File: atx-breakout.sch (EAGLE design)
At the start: 2 parts

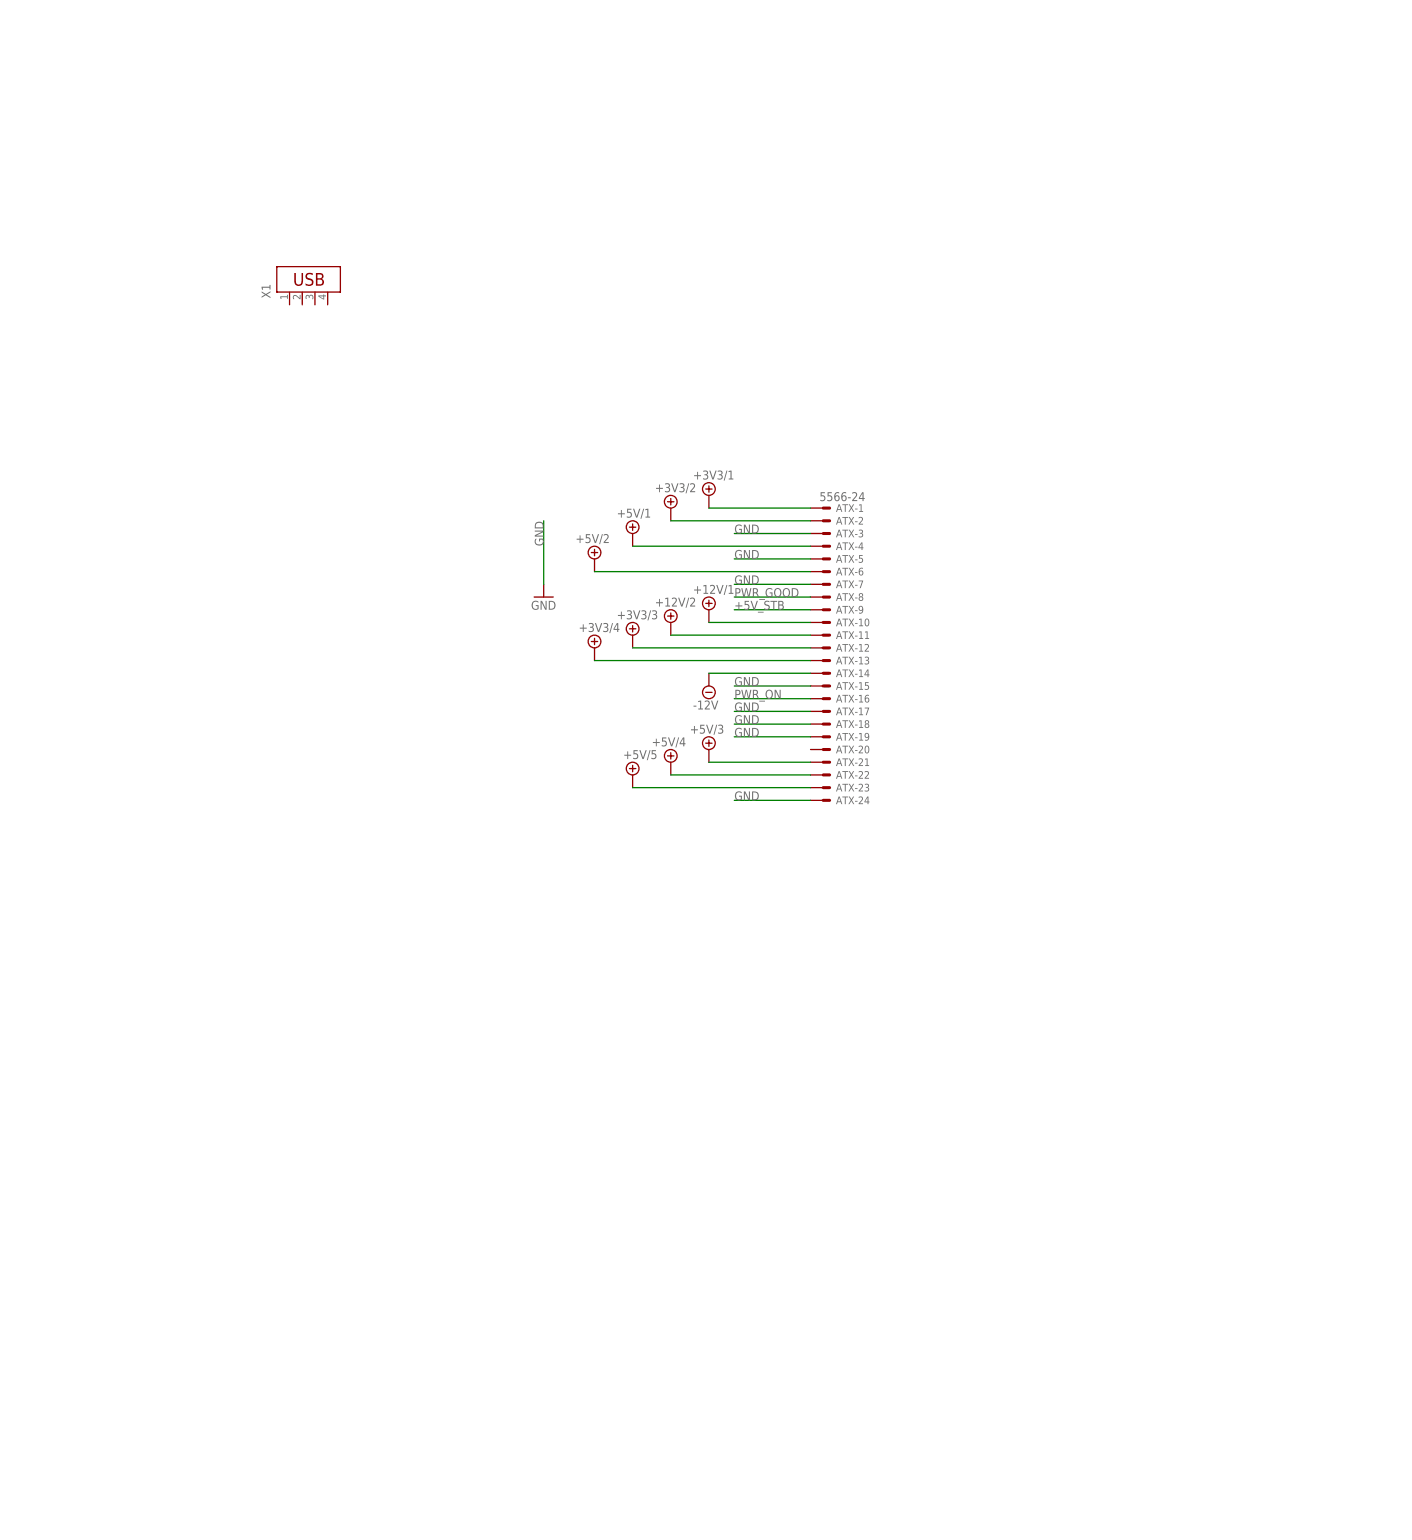
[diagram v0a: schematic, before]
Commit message: Six channel version, initial layout
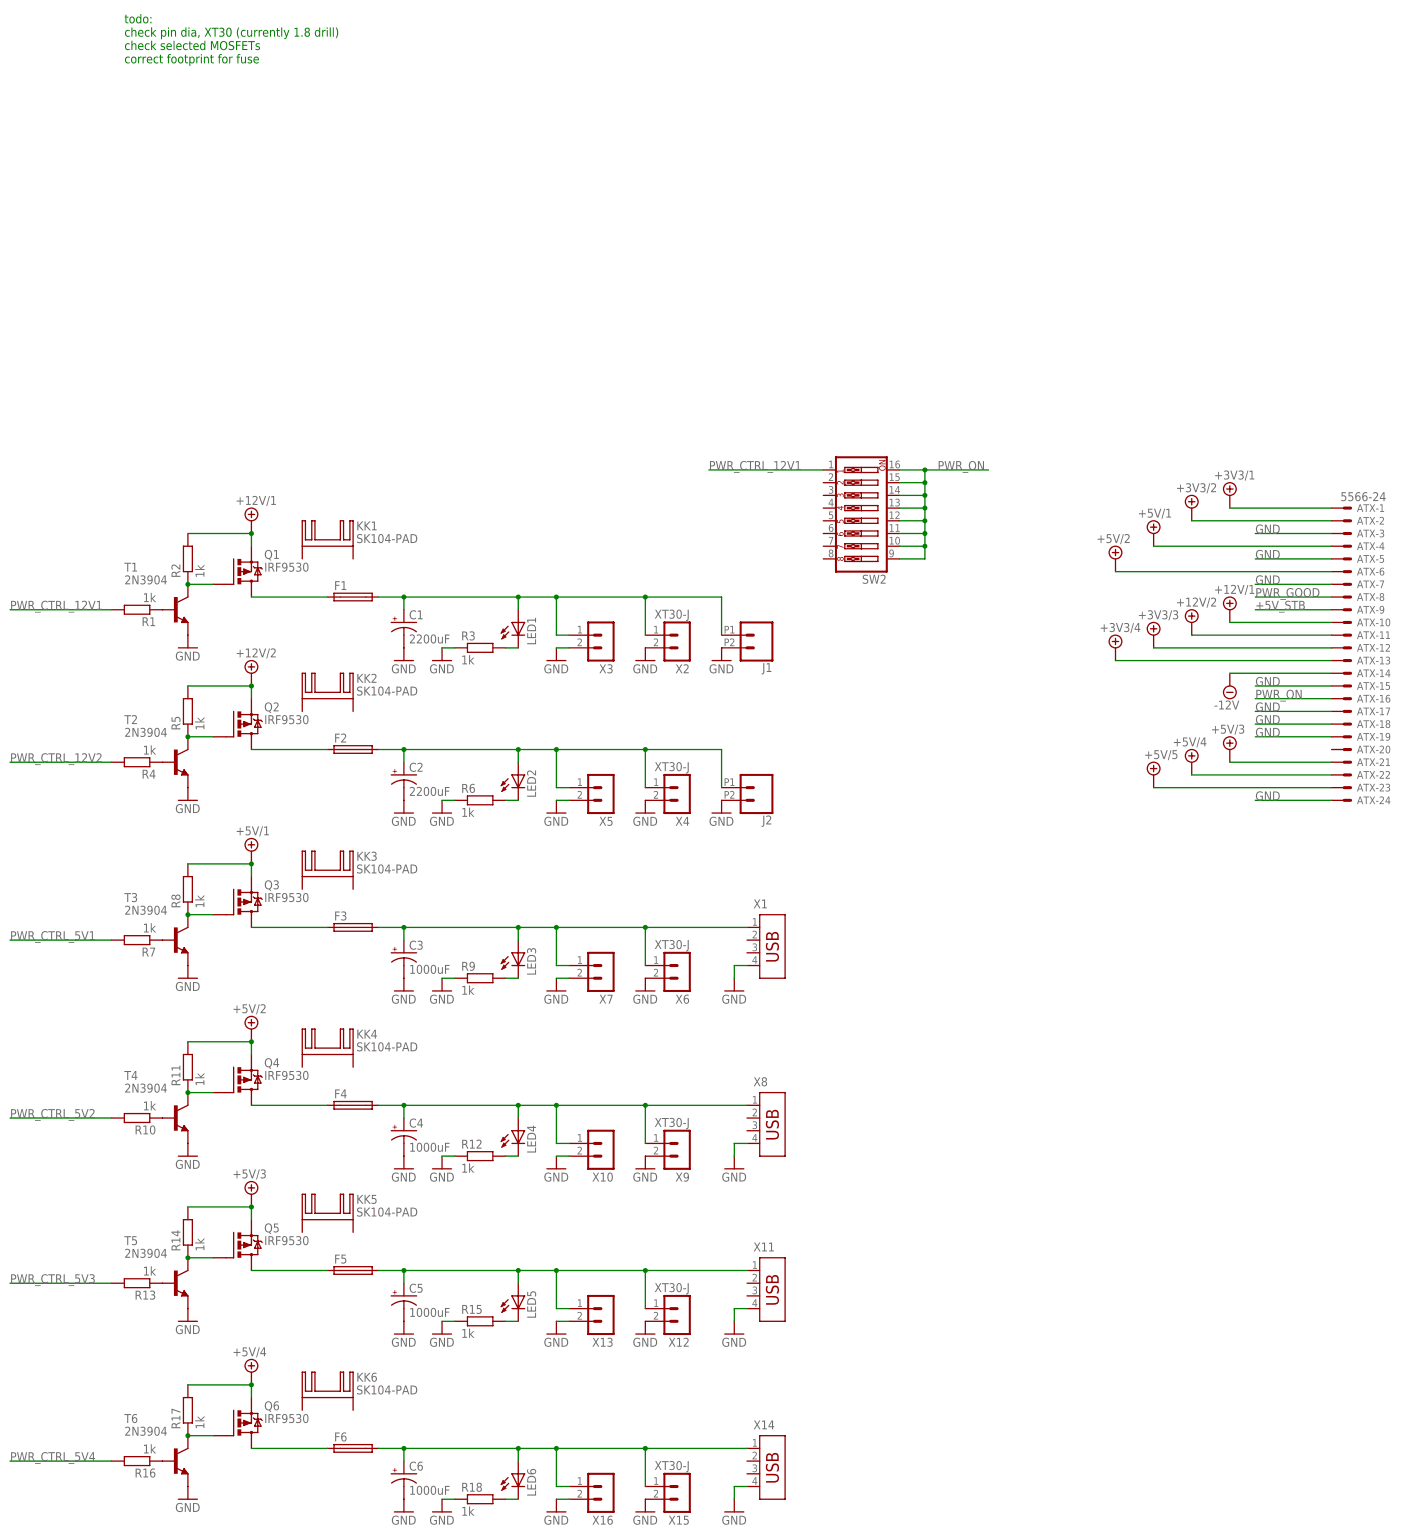
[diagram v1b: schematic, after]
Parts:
- added C1, C2: 2200uF, rcl:CPOL-USE7.5-16
- added C3, C4, C5, C6: 1000uF, rcl:CPOL-USE5-10.5
- added F1, F2, F3, F4, F5, F6: (no value), fuse:LITTLEFUSE
- added J1, J2: (no value), SparkFun-Connectors:CONN_022.54MM_SCREWTERM
- added KK1, KK2, KK3, KK4, KK5, KK6: SK104-PAD, heatsink:SK104-PAD
- added LED1, LED2, LED3, LED4, LED5, LED6: (no value), joakim:LED_J3MM
- added Q1, Q2, Q3, Q4, Q5, Q6: IRF9530, transistor-power:IRF9530
- added R1, R10, R11, R12, R13, R14, R15, R16, R17, R18, R2, R3, R4, R5, R6, R7, R8, R9: 1k, rcl:R-EU_0207/7
- added SW2: (no value), special:SW_DIP-8
- added T1, T2, T3, T4, T5, T6: 2N3904, transistor:2N3904
- added X10, X13, X16, X3, X5, X7: MA02-1JC, joakim:MA02-1JC
- added X11, X14, X8: (no value), con-amp:USB-787616
- added X12, X15, X2, X4, X6, X9: XT30-J, joakim:XT30-J
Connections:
- new net N$1: R1.1, T1.B
- new net N$10: LED2.C, R6.2
- new net N$11: F2.1, Q2.D
- new net N$12: R7.1, T3.B
- new net N$13: Q3.G, R8.1, T3.C
- new net N$14: C3.+, F3.2, LED3.A, X1.1, X6.1, X7.1
- new net N$15: LED3.C, R9.2
- new net N$16: F3.1, Q3.D
- new net N$17: R10.1, T4.B
- new net N$18: Q4.G, R11.1, T4.C
- new net N$19: C4.+, F4.2, LED4.A, X10.1, X8.1, X9.1
- new net N$2: Q1.G, R2.1, T1.C
- new net N$20: LED4.C, R12.2
- new net N$21: F4.1, Q4.D
- new net N$22: R13.1, T5.B
- new net N$23: Q5.G, R14.1, T5.C
- new net N$24: C5.+, F5.2, LED5.A, X11.1, X12.1, X13.1
- new net N$25: LED5.C, R15.2
- new net N$26: F5.1, Q5.D
- new net N$27: R16.1, T6.B
- new net N$28: Q6.G, R17.1, T6.C
- new net N$29: C6.+, F6.2, LED6.A, X14.1, X15.1, X16.1
- new net N$3: Q1.S, R2.2
- new net N$30: LED6.C, R18.2
- new net N$31: F6.1, Q6.D
- new net N$4: C1.+, F1.2, J1.1, LED1.A, X2.1, X3.1
- new net N$5: LED1.C, R3.2
- new net N$6: F1.1, Q1.D
- new net N$7: R4.1, T2.B
- new net N$8: Q2.G, R5.1, T2.C
- new net N$9: C2.+, F2.2, J2.1, LED2.A, X4.1, X5.1
- new net PWR_CTRL_12V1: R1.2, SW2.1
- new net PWR_CTRL_12V2: R4.2
- new net PWR_CTRL_5V1: R7.2
- new net PWR_CTRL_5V2: R10.2
- new net PWR_CTRL_5V3: R13.2
- new net PWR_CTRL_5V4: R16.2
- net +5V/1: now also Q2.S, Q3.S, R5.2, R8.2
- net +5V/2: now also Q4.S, R11.2
- net +5V/3: now also Q5.S, R14.2
- net +5V/4: now also Q6.S, R17.2
- net GND: now also C1.-, C2.-, C3.-, C4.-, C5.-, C6.-, J1.2, J2.2, R12.1, R15.1, R18.1, R3.1, R6.1, R9.1, T1.E, T2.E, T3.E, T4.E, T5.E, T6.E, X1.4, X10.2, X11.4, X12.2, X13.2, X14.4, X15.2, X16.2, X2.2, X3.2, X4.2, X5.2, X6.2, X7.2, X8.4, X9.2
- net PWR_ON: now also SW2.10, SW2.11, SW2.12, SW2.13, SW2.14, SW2.15, SW2.16, SW2.9
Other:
- note added: "todo: check pin dia, XT30 (currently 1.8 drill) check selected MOSFETs correct footprint for fuse"
- moved on the sheet: ATX-1, ATX-10, ATX-11, ATX-12, ATX-13, ATX-14, ATX-15, ATX-16, ATX-17, ATX-18, ATX-19, ATX-2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
